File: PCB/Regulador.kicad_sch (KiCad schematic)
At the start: 10 parts, among them J1 BAT- CONN, U3 lm1117-5V

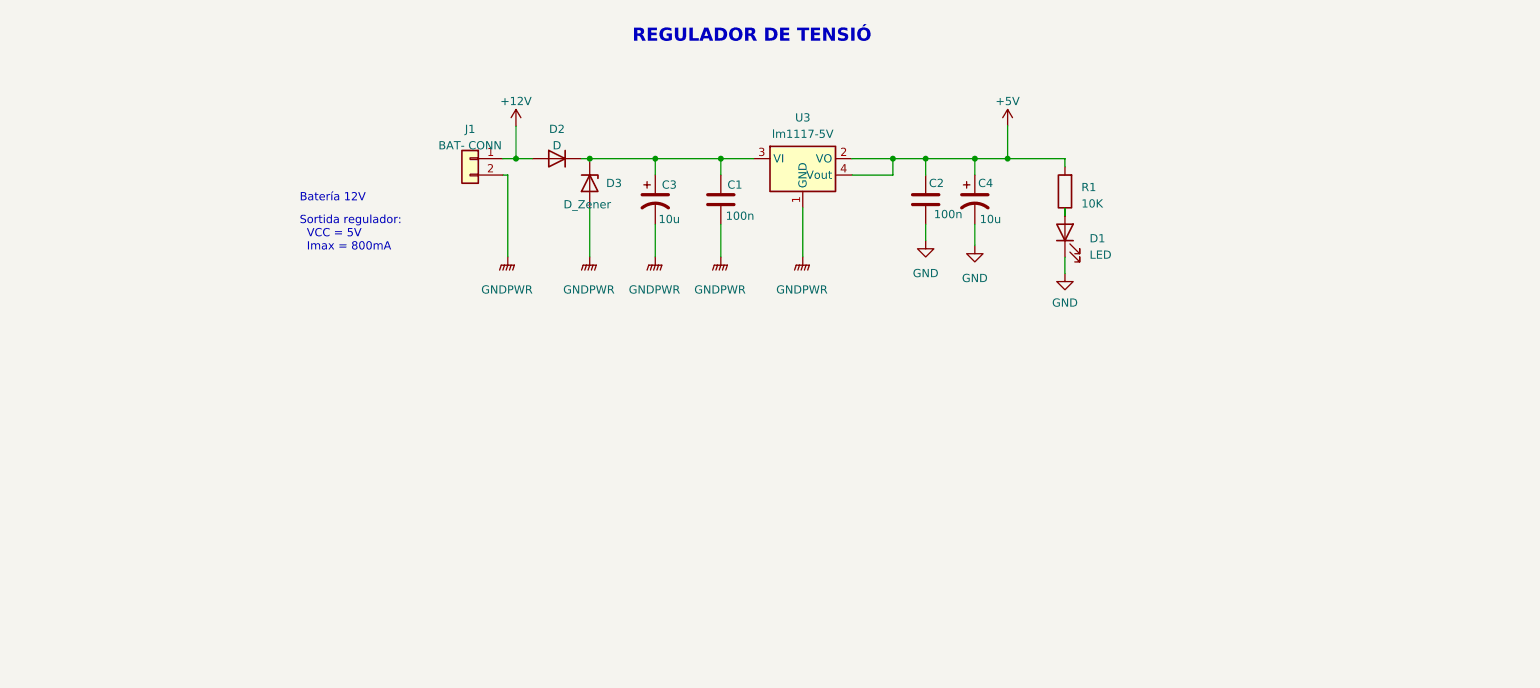
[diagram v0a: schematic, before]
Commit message: modificado el LM1117 a la versión TO-252 de 3 patas y salida no ajustable a 5V. Añadido el coil de salida 82683C para el BUCK a la librería
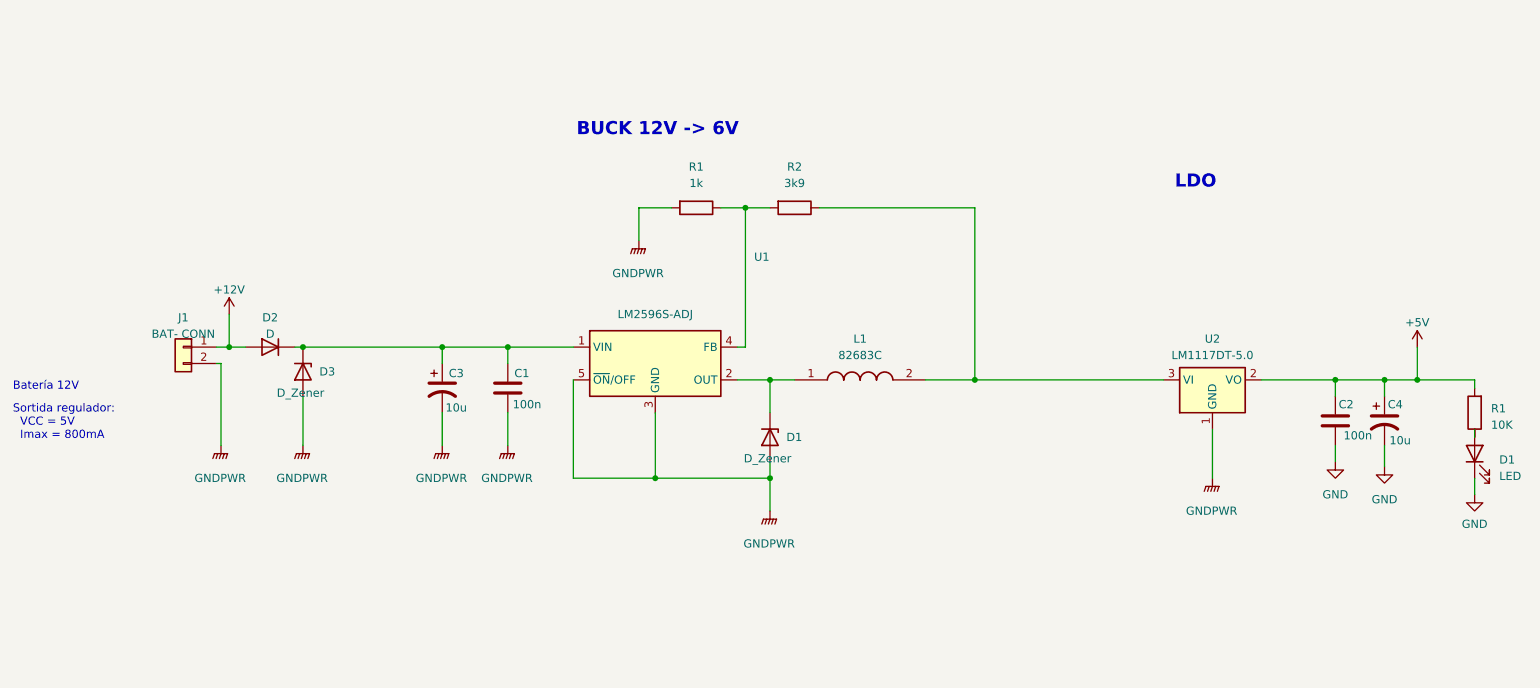
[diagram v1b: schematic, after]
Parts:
- removed U3: lm1117-5V, Package_TO_SOT_SMD:SOT-223-3_TabPin2, symbol David:AP1117-ADJ-mod
- added D1: D_Zener, Diode_THT:D_DO-15_P12.70mm_Horizontal, symbol Device:D_Zener
- added L1: 82683C, 82683C, symbol 82683C:82683C
- added R1: 1k, Resistor_SMD:R_1206_3216Metric_Pad1.30x1.75mm_HandSolder, symbol Device:R
- added R2: 3k9, Resistor_SMD:R_1206_3216Metric_Pad1.30x1.75mm_HandSolder, symbol Device:R
- added U1: LM2596S-ADJ, Package_TO_SOT_SMD:TO-263-5_TabPin3, symbol Regulator_Switching:LM2596S-ADJ
- added U2: LM1117DT-5.0, Package_TO_SOT_SMD:TO-252-3_TabPin2, symbol Regulator_Linear:LM1117DT-5.0
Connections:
- net +5V: now also U2.2 (VO)
- net GNDPWR: now also D1.2 (A), R1.2, U1.3 (GND), U1.5 (~{ON}/OFF), U2.1 (GND)
- net at C1.1, C3.1, D2.1 (K)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: now also U1.1 (VIN)
- new net: D1.1 (K), L1.1, U1.2 (OUT)
- new net: R1.1, R2.2, U1.4 (FB)
- new net: L1.2, R2.1, U2.3 (VI)
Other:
- note added: "BUCK 12V -> 6V"
- note added: "LDO"
- note removed: "REGULADOR DE TENSIÓ"
- moved on the sheet: C1, C2, C3, C4, D1, D2, D3, J1, R1

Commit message: anadido el shdn directo al PIC. Es un pin de alarma térmica del transceiver. El sensor de corriente está mal hay que darle una vuelta
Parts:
- renumbered D1 to D?, L1 to L?, R1 to R?, R2 to R?, U1 to U?, U2 to U?
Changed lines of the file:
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@@
 		(on_board yes)
 		(dnp no)
-		(property "Reference" "C?"
+		(property "Reference" "C2"
 			(at 236.728 96.52 0)
 			(effects
@@
 		(dnp no)
 		(fields_autoplaced yes)
-		(property "Reference" "J?"
+		(property "Reference" "J1"
 			(at 57.658 83.058 0)
 			(effects
@@
 		(on_board yes)
 		(dnp no)
-		(property "Reference" "U1"
+		(property "Reference" "U?"
 			(at 147.32 73.66 0)
 			(effects
@@
 		)
 		(instances
+			(project "puertas"
+				(path "/c96004bd-c0fc-431c-a510-eb1e1a82944f/e6b7430e-7a8c-411e-a7e4-bebdb17bd144"
+					(reference "U?")
+					(unit 1)
+				)
+			)
 			(project ""
 				(path "/f9cee2a8-0a19-4b11-9627-69569c878c91"
@@
 		(dnp no)
 		(fields_autoplaced yes)
-		(property "Reference" "#PWR?"
+		(property "Reference" "#PWR034"
 			(at 64.77 86.36 0)
 			(effects
@@
 		(dnp no)
 		(fields_autoplaced yes)
-		(property "Reference" "#PWR?"
+		(property "Reference" "#PWR04"
 			(at 243.84 112.522 0)
 			(effects
@@
 		(dnp no)
 		(fields_autoplaced yes)
-		(property "Reference" "L1"
+		(property "Reference" "L?"
 			(at 162.56 86.36 0)
 			(effects
@@
 		)
 		(instances
+			(project "puertas"
+				(path "/c96004bd-c0fc-431c-a510-eb1e1a82944f/e6b7430e-7a8c-411e-a7e4-bebdb17bd144"
+					(reference "L?")
+					(unit 1)
+				)
+			)
 			(project ""
 				(path "/f9cee2a8-0a19-4b11-9627-69569c878c91"
@@
 		(on_board yes)
 		(dnp no)
-		(property "Reference" "D1"
+		(property "Reference" "D?"
 			(at 151.13 101.6 90)
 			(effects
@@
 		)
 		(instances
+			(project "puertas"
+				(path "/c96004bd-c0fc-431c-a510-eb1e1a82944f/e6b7430e-7a8c-411e-a7e4-bebdb17bd144"
+					(reference "D?")
+					(unit 1)
+				)
+			)
 			(project "Regulador"
 				(path "/f9cee2a8-0a19-4b11-9627-69569c878c91"
@@
 		(on_board yes)
 		(dnp no)
-		(property "Reference" "C?"
+		(property "Reference" "C4"
 			(at 244.348 96.52 0)
 			(effects
@@
 		(dnp no)
 		(fields_autoplaced yes)
-		(property "Reference" "U2"
+		(property "Reference" "U?"
 			(at 217.17 86.36 0)
 			(effects
@@
 		)
 		(instances
+			(project "puertas"
+				(path "/c96004bd-c0fc-431c-a510-eb1e1a82944f/e6b7430e-7a8c-411e-a7e4-bebdb17bd144"
+					(reference "U?")
+					(unit 1)
+				)
+			)
 			(project ""
 				(path "/f9cee2a8-0a19-4b11-9627-69569c878c91"
@@
 		(on_board yes)
 		(dnp no)
-		(property "Reference" "#PWR?"
+		(property "Reference" "#PWR06"
 			(at 248.92 91.44 0)
 			(effects
@@
 		(on_board yes)
 		(dnp no)
-		(property "Reference" "D?"
+		(property "Reference" "D3"
 			(at 78.74 91.44 90)
 			(effects
@@
 		(dnp no)
 		(fields_autoplaced yes)
-		(property "Reference" "#PWR?"
+		(property "Reference" "#PWR01"
 			(at 217.17 113.03 0)
 			(effects
@@
 		(dnp no)
 		(fields_autoplaced yes)
-		(property "Reference" "#PWR02"
+		(property "Reference" "#PWR0105"
 			(at 128.27 76.2 0)
 			(effects
@@
 		)
 		(instances
+			(project "puertas"
+				(path "/c96004bd-c0fc-431c-a510-eb1e1a82944f/e6b7430e-7a8c-411e-a7e4-bebdb17bd144"
+					(reference "#PWR0105")
+					(unit 1)
+				)
+			)
 			(project "Regulador"
 				(path "/f9cee2a8-0a19-4b11-9627-69569c878c91"
@@
 		(dnp no)
 		(fields_autoplaced yes)
-		(property "Reference" "#PWR?"
+		(property "Reference" "#PWR02"
 			(at 107.95 107.95 0)
 			(effects
@@
 		(dnp no)
 		(fields_autoplaced yes)
-		(property "Reference" "R?"
+		(property "Reference" "R1"
 			(at 260.35 97.155 0)
 			(effects
@@
 		(on_board yes)
 		(dnp no)
-		(property "Reference" "C?"
+		(property "Reference" "C3"
 			(at 98.806 91.694 0)
 			(effects
@@
 		(on_board yes)
 		(dnp no)
-		(property "Reference" "#PWR?"
+		(property "Reference" "#PWR09"
 			(at 257.81 116.84 0)
 			(effects
@@
 		(dnp no)
 		(fields_autoplaced yes)
-		(property "Reference" "D?"
+		(property "Reference" "D1"
 			(at 261.62 105.0925 90)
 			(effects
@@
 		(on_board yes)
 		(dnp no)
-		(property "Reference" "C?"
+		(property "Reference" "C1"
 			(at 108.966 91.694 0)
 			(effects
@@
 		(dnp no)
 		(fields_autoplaced yes)
-		(property "Reference" "#PWR01"
+		(property "Reference" "#PWR0106"
 			(at 148.59 118.11 0)
 			(effects
@@
 		)
 		(instances
+			(project "puertas"
+				(path "/c96004bd-c0fc-431c-a510-eb1e1a82944f/e6b7430e-7a8c-411e-a7e4-bebdb17bd144"
+					(reference "#PWR0106")
+					(unit 1)
+				)
+			)
 			(project "Regulador"
 				(path "/f9cee2a8-0a19-4b11-9627-69569c878c91"
@@
 		(dnp no)
 		(fields_autoplaced yes)
-		(property "Reference" "D?"
+		(property "Reference" "D2"
 			(at 71.12 83.058 0)
 			(effects
@@
 		(dnp no)
 		(fields_autoplaced yes)
-		(property "Reference" "#PWR?"
+		(property "Reference" "#PWR07"
 			(at 76.2 107.95 0)
 			(effects
@@
 		(dnp no)
 		(fields_autoplaced yes)
-		(property "Reference" "#PWR?"
+		(property "Reference" "#PWR05"
 			(at 97.79 107.95 0)
 			(effects
@@
 		(dnp no)
 		(fields_autoplaced yes)
-		(property "Reference" "R1"
+		(property "Reference" "R?"
 			(at 137.16 59.69 90)
 			(effects
@@
 		)
 		(instances
+			(project "puertas"
+				(path "/c96004bd-c0fc-431c-a510-eb1e1a82944f/e6b7430e-7a8c-411e-a7e4-bebdb17bd144"
+					(reference "R?")
+					(unit 1)
+				)
+			)
 			(project "Regulador"
 				(path "/f9cee2a8-0a19-4b11-9627-69569c878c91"
@@
 		(dnp no)
 		(fields_autoplaced yes)
-		(property "Reference" "R2"
+		(property "Reference" "R?"
 			(at 152.4 59.69 90)
 			(effects
@@
 		)
 		(instances
+			(project "puertas"
+				(path "/c96004bd-c0fc-431c-a510-eb1e1a82944f/e6b7430e-7a8c-411e-a7e4-bebdb17bd144"
+					(reference "R?")
+					(unit 1)
+				)
+			)
 			(project "Regulador"
 				(path "/f9cee2a8-0a19-4b11-9627-69569c878c91"
@@
 		(dnp no)
 		(fields_autoplaced yes)
-		(property "Reference" "#PWR?"
+		(property "Reference" "#PWR03"
 			(at 236.22 111.76 0)
 			(effects
@@
 		(dnp no)
 		(fields_autoplaced yes)
-		(property "Reference" "#PWR?"
+		(property "Reference" "#PWR060"
 			(at 63.5 107.95 0)
 			(effects

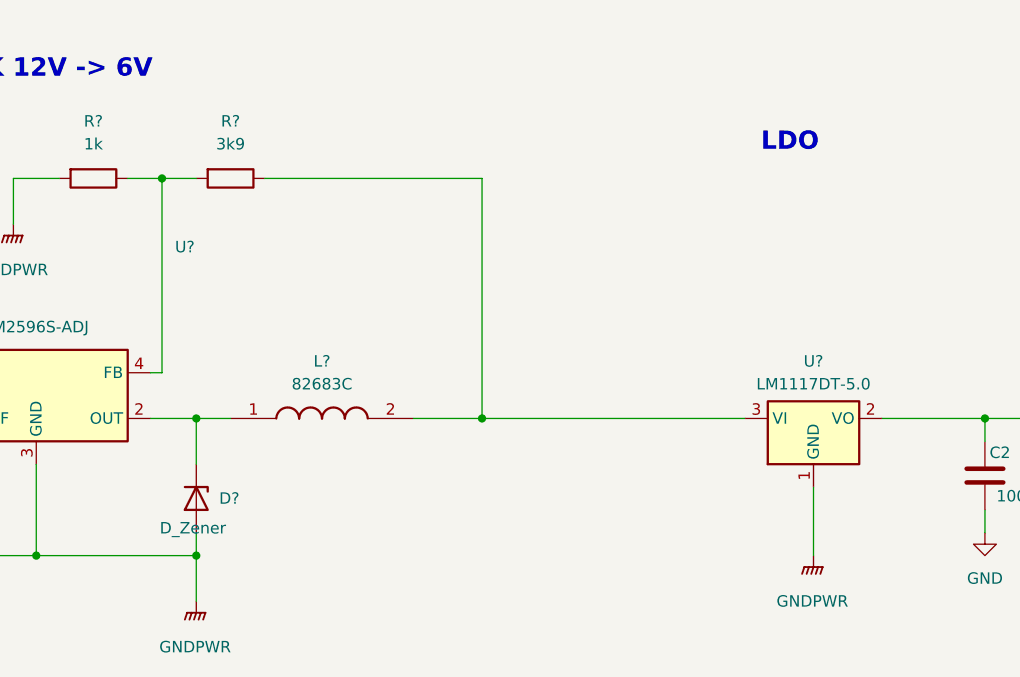
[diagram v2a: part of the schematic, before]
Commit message: Condesnadors buck converter
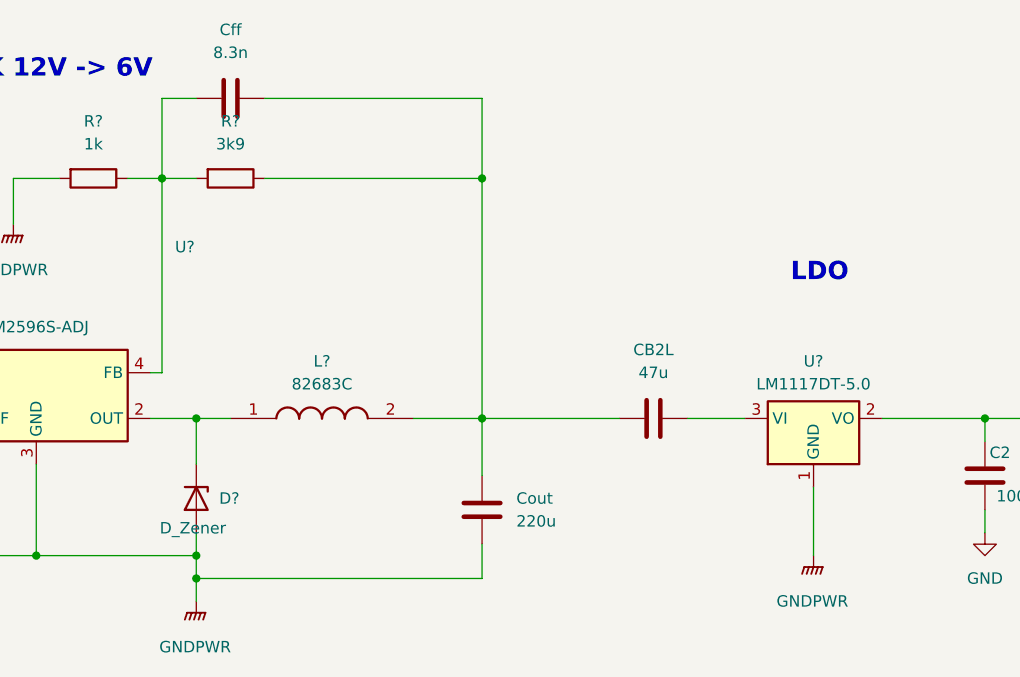
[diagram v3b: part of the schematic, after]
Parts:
- added CB2L: 47u, symbol Device:C
- added Cff: 8.3n, symbol Device:C
- added Cout: 220u, symbol Device:C
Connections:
- net GNDPWR: now also Cout.2
- net at R?.1, R?.2, U?.4 (FB): now also Cff.1
- net at L?.2, R?.1: now also CB2L.1, Cff.2, Cout.1; no longer U?.3 (VI)
- new net: CB2L.2, U?.3 (VI)

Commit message: Add files via upload
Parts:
- removed CB2L: 47u, symbol Device:C
- removed Cff: 8.3n, symbol Device:C
- removed Cout: 220u, symbol Device:C
- removed D?: D_Zener, Diode_THT:D_DO-15_P12.70mm_Horizontal, symbol Device:D_Zener
- removed J1: BAT- CONN, Connector_PinHeader_2.54mm:PinHeader_1x02_P2.54mm_Vertical, symbol Connector_Generic:Conn_01x02
- removed L?: 82683C, 82683C, symbol 82683C:82683C
- removed R?: 1k, Resistor_SMD:R_1206_3216Metric_Pad1.30x1.75mm_HandSolder, symbol Device:R
- removed R?: 3k9, Resistor_SMD:R_1206_3216Metric_Pad1.30x1.75mm_HandSolder, symbol Device:R
- removed U?: LM2596S-ADJ, Package_TO_SOT_SMD:TO-263-5_TabPin3, symbol Regulator_Switching:LM2596S-ADJ
- removed U?: LM1117DT-5.0, Package_TO_SOT_SMD:TO-252-3_TabPin2, symbol Regulator_Linear:LM1117DT-5.0
- added C12: 1uF, Capacitor_SMD:C_0805_2012Metric, symbol Device:C_Polarized_US
- added C8: 100n, Capacitor_SMD:C_1206_3216Metric, symbol Device:C
- added J5: BAT_CONN, TerminalBlock_Phoenix:TerminalBlock_Phoenix_MPT-0,5-2-2.54_1x02_P2.54mm_Horizontal, symbol Connector:Screw_Terminal_01x02
- added R10: 0, Capacitor_SMD:C_1206_3216Metric, symbol Device:R
- added U2: lm1117-5V, Package_TO_SOT_SMD:SOT-223-3_TabPin2, symbol David:AP1117-ADJ-mod
- added U3: LT1121IST-3.3-TRPBF, LT1121IST:SOT-223_ST_LIT, symbol LT1121IST:LT1121IST-3.3-TRPBF
- C3, C4: footprint Capacitor_THT:CP_Radial_D6.3mm_P2.50mm -> Capacitor_THT:CP_Radial_D5.0mm_P2.50mm
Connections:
- net +12V: now also J5.1 (Pin_1)
- net +5V: now also C8.1, U2.2 (VO), U2.4 (Vout), U3.1 (VIN)
- net GND: now also C12.2, C8.2, R10.2, U3.2 (GND)
- net GNDPWR: now also J5.2 (Pin_2), R10.1, U2.1 (GND)
- net at C1.1, C3.1, D2.1 (K)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: now also U2.3 (VI)
- new net +3.3V: C12.1, U3.3 (OUTPUT)
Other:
- note added: "REGULADOR DE TENSIÓN 3.3V"
- note added: "REGULADOR DE TENSIÓN LINEAL"
- note added: "SEPARACIÓN DE GNDs"
- note removed: "BUCK 12V -> 6V"
- note removed: "LDO"
- moved on the sheet: C1, C2, C3, C4, D1, D2, D3, R1

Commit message: esquemático  v2
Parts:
- D1: footprint LED_SMD:LED_0805_2012Metric -> (none)
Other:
- moved on the sheet: C1, C12, C2, C3, C4, C8, D2, D3, J5, R1, R10, U2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

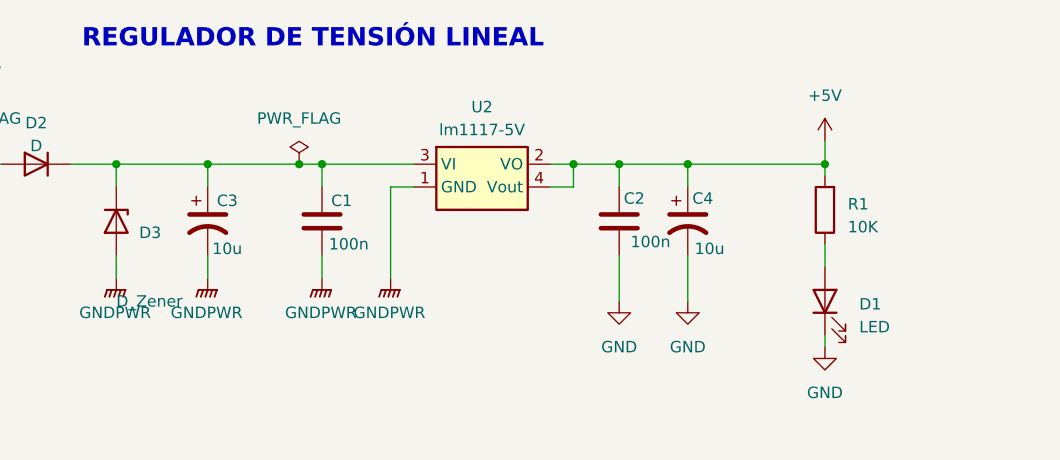
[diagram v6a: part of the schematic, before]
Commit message: corrección de error de grid
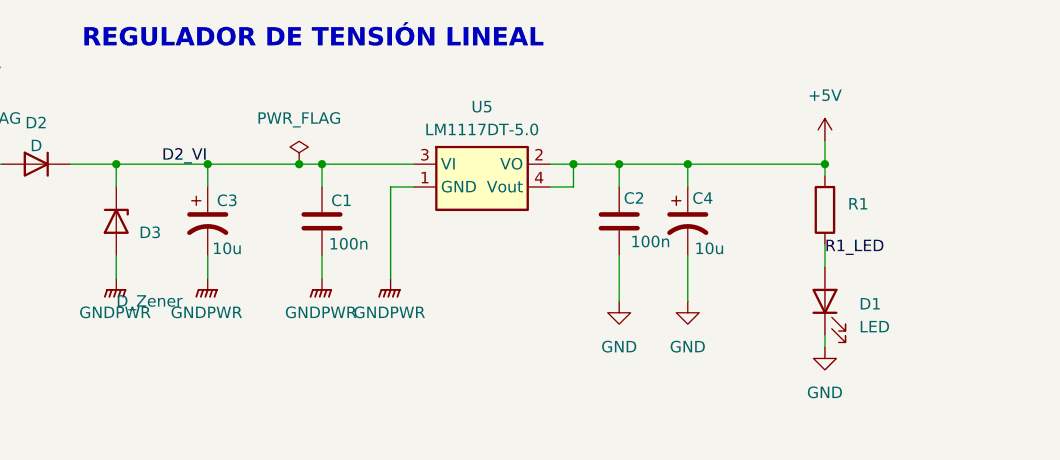
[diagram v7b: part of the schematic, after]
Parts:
- removed U2: lm1117-5V, Package_TO_SOT_SMD:SOT-223-3_TabPin2, symbol David:AP1117-ADJ-mod
- added U5: LM1117DT-5.0, Package_TO_SOT_SMD:TO-252-3_TabPin2, symbol Regulator_Linear:LM1117DT-5.0
- D1: footprint (none) -> LED_SMD:LED_1206_3216Metric
- J5: footprint TerminalBlock_Phoenix:TerminalBlock_Phoenix_MPT-0,5-2-2.54_1x02_P2.54mm_Horizontal -> TerminalBlock_Phoenix:TerminalBlock_Phoenix_MKDS-3-2-5.08_1x02_P5.08mm_Horizontal
- U3: footprint LT1121IST:SOT-223_ST_LIT -> Package_TO_SOT_SMD:SOT-223-3_TabPin2
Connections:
- net +5V: now also U5.2 (VO), U5.4 (Vout)
- net GNDPWR: now also U5.1 (GND)
- net R1_LED: now reaches D1.2 (A), R1.1
- net D2_VI: now reaches C1.1, C3.1, D2.1 (K), D3.1 (K)
- net D2_VI: now also U5.3 (VI)
